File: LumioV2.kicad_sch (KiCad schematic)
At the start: 28 parts, among them J1 Raspi 5, J10 US Dist - Back, J2 I2C POINT 1 - QWIIC, J3 I2C POINT 2 - QWIIC, J4 I2C POINT 3 - JST-PH, J5 Display Connector, J6 MOTOR A, J7 MOTOR B, J8 I2C POINT 4 - JST-PH, J9 US Dist - Front, U1 L298N, U2 LM2577T-ADJ/NOPB

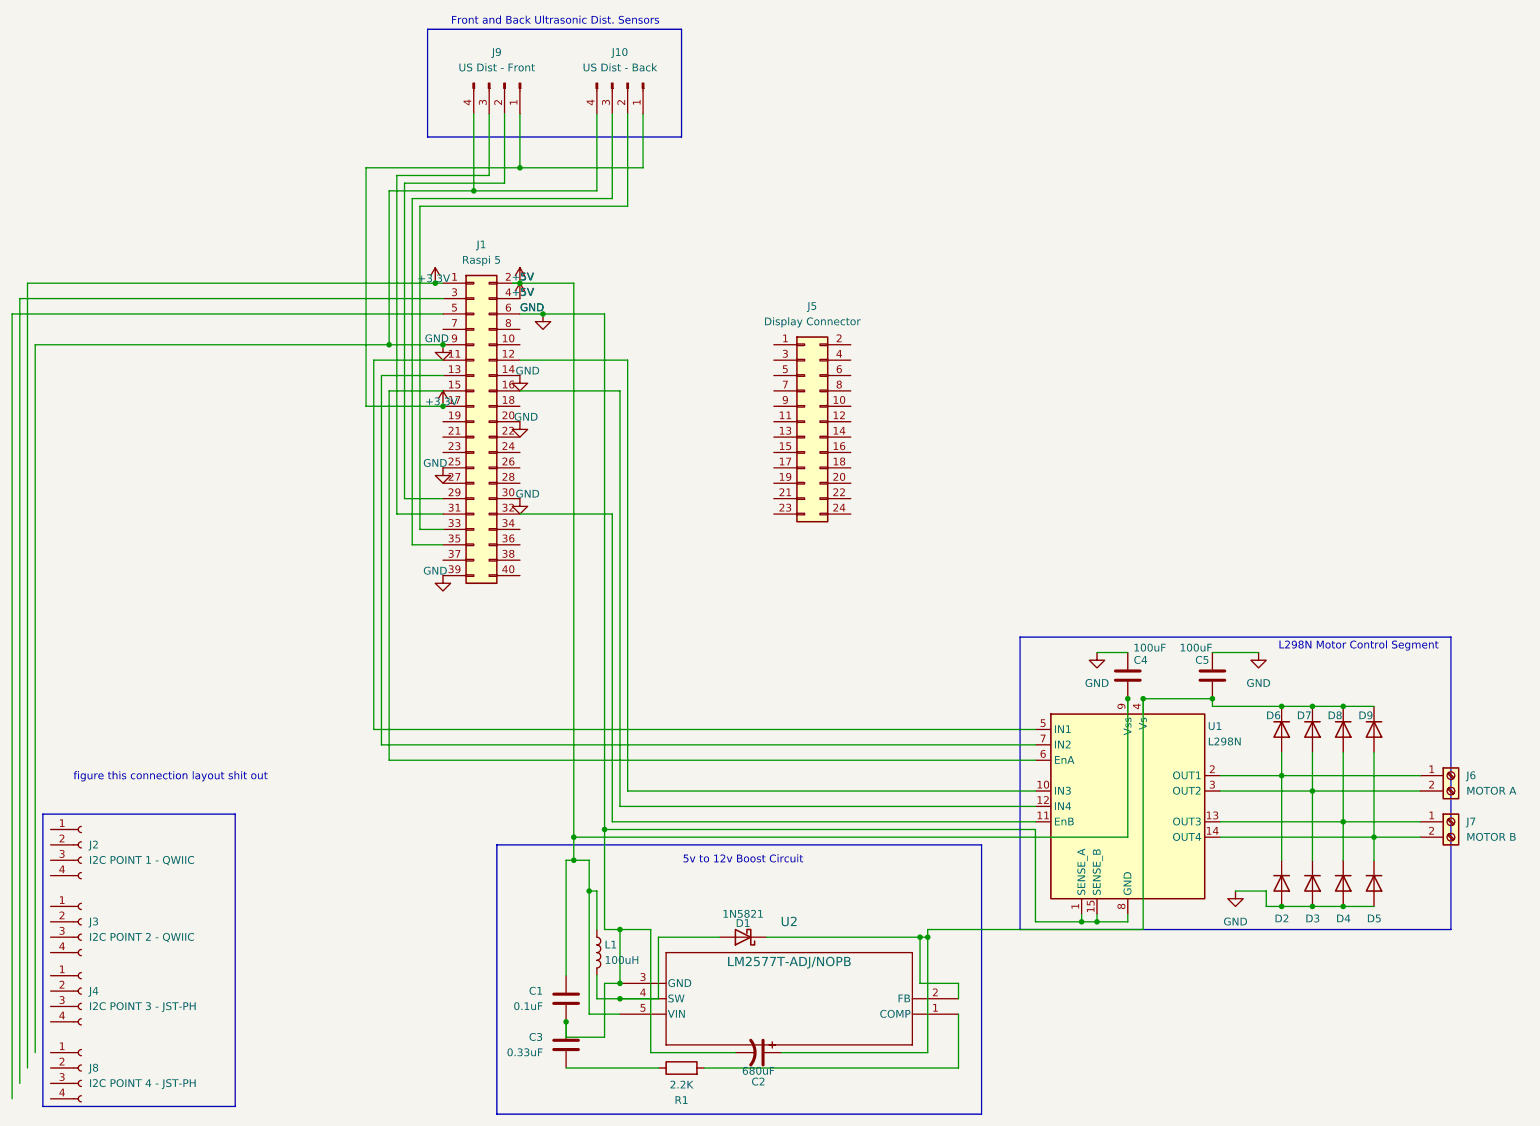
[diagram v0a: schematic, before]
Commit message: Routed display connector,
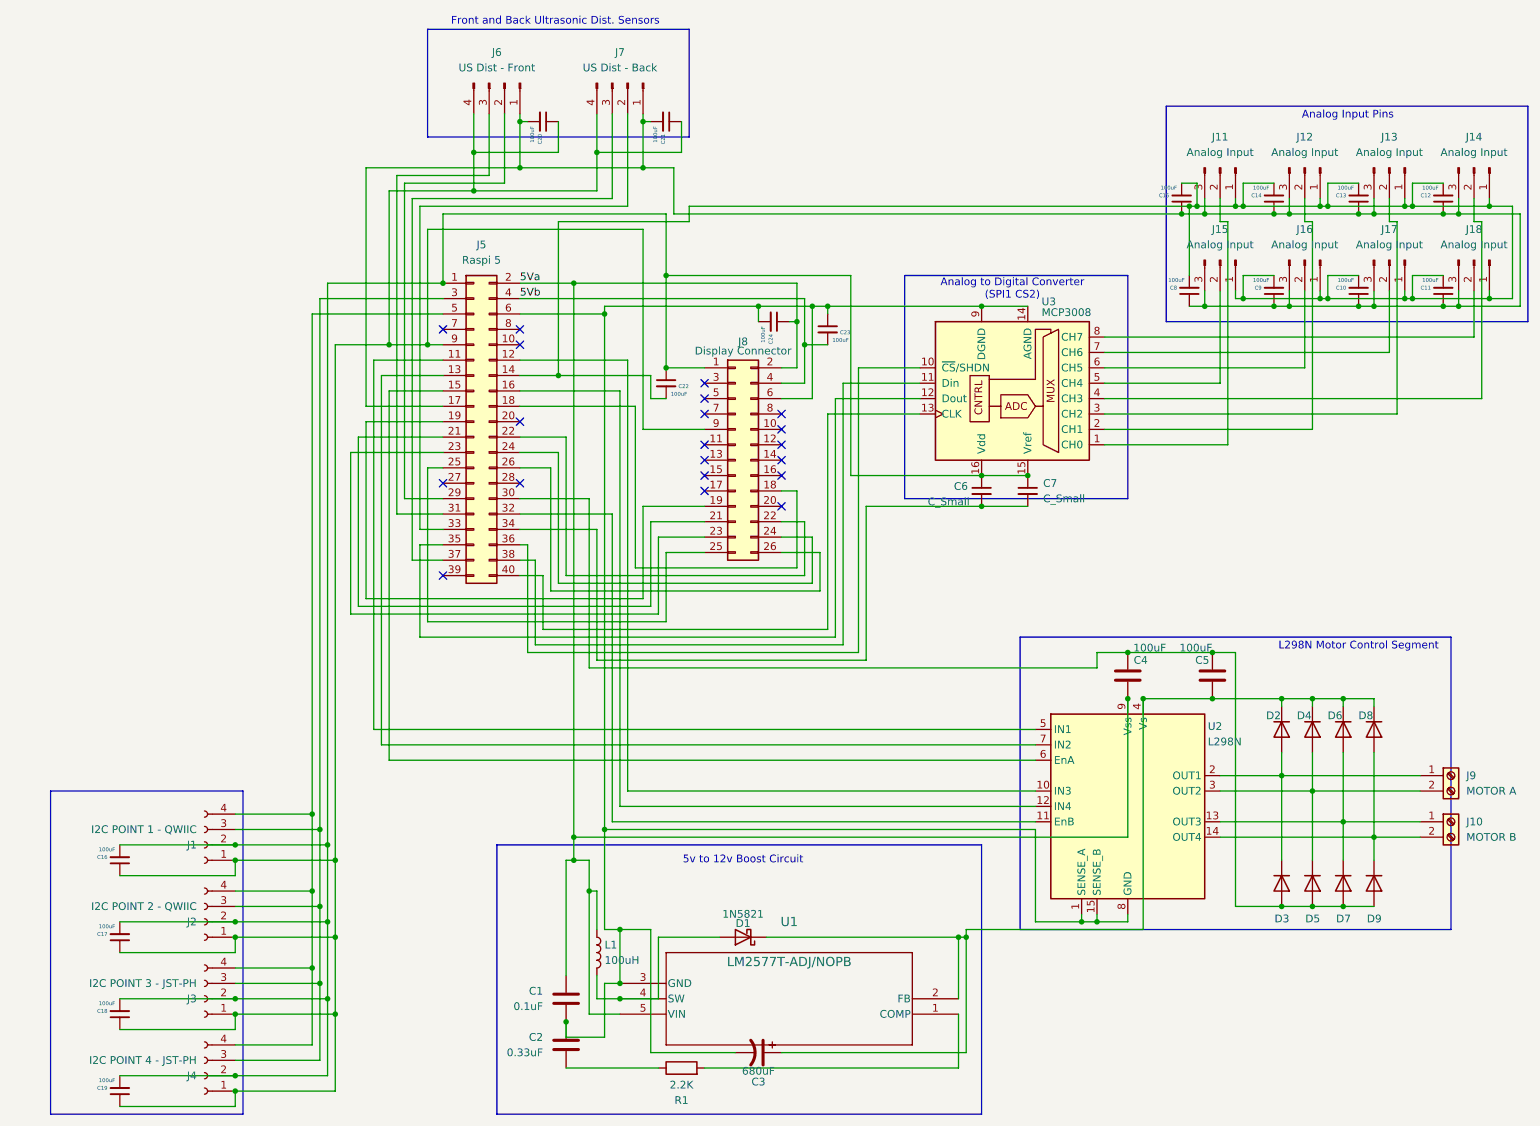
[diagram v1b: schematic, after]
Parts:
- removed J5: Display Connector, Connector_PinHeader_1.00mm:PinHeader_2x12_P1.00mm_Vertical, symbol Connector_Generic:Conn_02x12_Odd_Even
- added C10, C11, C12, C13, C14, C15, C16, C17, C18, C19, C20, C21, C22, C23, C24, C8, C9: 100uF, symbol Device:C_Small
- added C6, C7: C_Small, symbol Device:C_Small
- added J11, J12, J13, J14, J15, J16, J17, J18: Analog Input, symbol Connector:Conn_01x03_Pin
- added J8: Display Connector, symbol Connector_Generic:Conn_02x13_Odd_Even
- added U3: MCP3008, symbol Analog_ADC:MCP3008
- renumbered C3 to C2, C2 to C3, D6 to D2, D2 to D3, D7 to D4, D3 to D5, D8 to D6, D4 to D7, D9 to D8, D5 to D9, J2 to J1, J7 to J10, J3 to J2, J4 to J3, J8 to J4, J1 to J5, J9 to J6, J10 to J7, J6 to J9, U2 to U1, U1 to U2
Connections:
- net at J3.1 (Pin_1): now also J1.1 (Pin_1), J2.1 (Pin_1), J4.1 (Pin_1), J5.9 (Pin_9), J6.4 (Pin_4), J7.4 (Pin_4), C16.1, C17.1, C18.1, C19.1, C20.1, C21.1, J8.9 (Pin_9)
- net at J3.2 (Pin_2): now also J1.2 (Pin_2), J2.2 (Pin_2), J4.2 (Pin_2), J5.1 (Pin_1), C16.2, C17.2, C18.2, C19.2, C22.1, C6.1, C7.1, J8.1 (Pin_1), U3.15 (Vref), U3.16 (Vdd)
- net at J3.3 (Pin_3): now also J1.3 (Pin_3), J2.3 (Pin_3), J4.3 (Pin_3), J5.3 (Pin_3)
- net at J3.4 (Pin_4): now also J1.4 (Pin_4), J2.4 (Pin_4), J4.4 (Pin_4), J5.5 (Pin_5)
- net at J5.18 (Pin_18): now also J8.18 (Pin_18)
- net at J5.19 (Pin_19): now also J8.19 (Pin_19)
- net at J5.21 (Pin_21): now also J8.21 (Pin_21)
- net at J5.22 (Pin_22): now also J8.22 (Pin_22)
- net at J5.23 (Pin_23): now also J8.23 (Pin_23)
- net at J5.24 (Pin_24): now also J8.24 (Pin_24)
- net at J5.26 (Pin_26): now also J8.26 (Pin_26)
- net at J5.34 (Pin_34): now also C6.2, C7.2
- net at J5.35 (Pin_35): now also U3.12 (Dout); no longer J7.3 (Pin_3)
- net at J5.36 (Pin_36): now also U3.10 (~{CS}/SHDN)
- net at J5.37 (Pin_37): now also J7.3 (Pin_3)
- net at J5.38 (Pin_38): now also U3.11 (Din)
- net at J5.40 (Pin_40): now also U3.13 (CLK)
- net +3.3V: no longer names the net of J5.17 (Pin_17), J6.1 (Pin_1), J7.1 (Pin_1)
- net +3.3V: now also C10.1, C11.1, C12.1, C13.1, C14.1, C15.1, C20.2, C21.2, C8.1, C9.1, J11.3 (Pin_3), J12.3 (Pin_3), J13.3 (Pin_3), J14.3 (Pin_3), J15.3 (Pin_3), J16.3 (Pin_3), J17.3 (Pin_3), J18.3 (Pin_3); no longer J5.1 (Pin_1)
- net +5V renamed 5Va
- net 5Va: now also C24.1, J8.2 (Pin_2); no longer J5.4 (Pin_4)
- removed net GND: C1.2, C2.1, C3.2, C4.1, C5.1, D3.2 (A), D5.2 (A), D7.2 (A), D9.2 (A), J5.14 (Pin_14), J5.20 (Pin_20), J5.25 (Pin_25), J5.30 (Pin_30), J5.39 (Pin_39), J5.6 (Pin_6), J5.9 (Pin_9), J6.4 (Pin_4), J7.4 (Pin_4), U1.3 (GND), U2.1 (SENSE_A), U2.15 (SENSE_B), U2.8 (GND)
- new net: C10.2, C11.2, C12.2, C13.2, C14.2, C15.2, C22.2, C8.2, C9.2, J11.1 (Pin_1), J12.1 (Pin_1), J13.1 (Pin_1), J14.1 (Pin_1), J15.1 (Pin_1), J16.1 (Pin_1), J17.1 (Pin_1), J18.1 (Pin_1), J5.14 (Pin_14)
- new net: C1.2, C2.1, C23.1, C24.2, C3.2, J5.6 (Pin_6), J8.6 (Pin_6), U1.3 (GND), U2.1 (SENSE_A), U2.15 (SENSE_B), U2.8 (GND), U3.14 (AGND), U3.9 (DGND)
- new net: C4.1, C5.1, D3.2 (A), D5.2 (A), D7.2 (A), D9.2 (A), J5.30 (Pin_30)
- new net: J11.2 (Pin_2), U3.1 (CH0)
- new net: J12.2 (Pin_2), U3.2 (CH1)
- new net: J13.2 (Pin_2), U3.3 (CH2)
- new net: J14.2 (Pin_2), U3.4 (CH3)
- new net: J15.2 (Pin_2), U3.5 (CH4)
- new net: J16.2 (Pin_2), U3.6 (CH5)
- new net: J17.2 (Pin_2), U3.7 (CH6)
- new net: J18.2 (Pin_2), U3.8 (CH7)
- new net: J5.25 (Pin_25), J8.25 (Pin_25)
- new net 5Vb: C23.2, J5.4 (Pin_4), J8.4 (Pin_4)
- no-connect marks 0 -> 20
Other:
- note added: "Analog Input Pins"
- note added: "Analog to Digital Converter (SPI1 CS2)"
- note removed: "figure this connection layout shit out"
- moved on the sheet: J1, J2, J3, J4
